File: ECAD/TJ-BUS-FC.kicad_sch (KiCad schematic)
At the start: 31 parts

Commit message: teensy lib
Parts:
- removed A?: (no value), symbol 9602N:9602N
- removed AE?: (no value), symbol Device:Antenna_Shield
- removed C? (x8): (no value), symbol Device:C
- removed C? (x2): (no value), symbol Device:C_Polarized
- removed L?: (no value), symbol Device:L
- removed R? (x2): (no value), symbol Device:R
- removed TP? (x2): (no value), symbol Connector:TestPoint
- removed TP? (x2): (no value), symbol Connector:TestPoint_2Pole
- removed U?: (no value), symbol Amplifier_Current:INA138
- removed U?: (no value), symbol Symbols:MAX17644
- added U?: Teensy4.1, symbol teensy:Teensy4.1
- added U?: DS3232M, Package_SO:SOIC-8_3.9x4.9mm_P1.27mm, symbol Timer_RTC:DS3232M
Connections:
- no-connect marks 11 -> 8
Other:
- added sheet Radio (Iridium.kicad_sch)
- note removed: "750KHz selected"
- note removed: "8ms soft start"
- note removed: "All logic is 3.3V logic level, but is 5V tolerant TX and RX are from master device (TX is input to the 9602, RX is output from the 9602)"
- note removed: "DCM Mode"
- note removed: "Low ESR MLCC + Tantalum Bulk Capacitance"
- note removed: "Probe here to check internal 3V3"
- note removed: "Specced 18V max input"
- note removed: "Synchronous Buck - Stable 5V Out, 2.7A current limit"
- note removed: "This thing is really picky about power: 5V, <100mVpp 0-50KHz, <10mVpp 1MHz, <5mVpp 5Mhz Transients spikes during xmit from 40mA (idle) to 1.5A (xmit) for 8.3ms Cannot droop below 4.8V during this time OCP required, and in-rush current limit to 4A"

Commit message: bno055
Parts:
- added U?: (no value), symbol Symbols:Adafruit BNO055
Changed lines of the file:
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@@
     (pin "8")
+  )
+  (symbol (lib_id "Symbols:Adafruit BNO055") (at 207.01 69.85 0) (unit 1)
+    (in_bom yes) (on_board yes) (fields_autoplaced)
+    (property "Reference" "U?" (id 0) (at 207.01 64.77 0))
+    (property "Value" "" (id 1) (at 207.01 67.31 0))
+    (property "Footprint" "" (id 2) (at 207.01 69.85 0)
+      (effects (font (size 1.27 1.27)) hide)
+    )
+    (property "Datasheet" "" (id 3) (at 207.01 69.85 0)
+      (effects (font (size 1.27 1.27)) hide)
+    )
+    (pin "1")
+    (pin "10")
+    (pin "2")
+    (pin "3")
+    (pin "4")
+    (pin "5")
+    (pin "6")
+    (pin "7")
+    (pin "8")
+    (pin "9")
   )
   (sheet (at 238.76 30.48) (size 20.32 10.16) (fields_autoplaced)
@@
       (reference "U?") (unit 1) (value "DS3232M") (footprint "Package_SO:SOIC-8_3.9x4.9mm_P1.27mm")
     )
-  )
+    (path "/cfd6d7d9-e276-49ef-829b-32515e258b69"
+      (reference "U?") (unit 1) (value "Adafruit BNO055") (footprint "")
+    )
+  )

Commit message: changes
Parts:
- U?: value (none) -> Adafruit BNO055
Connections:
- net +5V: now also U?.48 (VIN)
- net at U?.34 (GND): now also U?.47 (GND)
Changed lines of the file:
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@@
   (no_connect (at 327.66 96.52))
   (no_connect (at 327.66 76.2))
+  (wire (pts (xy 54.61 55.88) (xy 59.69 55.88))
+    (stroke (width 0) (type default) (color 0 0 0 0))
+  )
   (wire (pts (xy 306.07 73.66) (xy 306.07 83.82))
     (stroke (width 0) (type default) (color 0 0 0 0))
@@
     (stroke (width 0) (type default) (color 0 0 0 0))
   )
+  (wire (pts (xy 115.57 55.88) (xy 119.38 55.88))
+    (stroke (width 0) (type default) (color 0 0 0 0))
+  )
+  (wire (pts (xy 115.57 91.44) (xy 133.35 91.44))
+    (stroke (width 0) (type default) (color 0 0 0 0))
+  )
   (wire (pts (xy 327.66 86.36) (xy 336.55 86.36))
     (stroke (width 0) (type default) (color 0 0 0 0))
@@
     (stroke (width 0) (type default) (color 0 0 0 0))
   )
+  (wire (pts (xy 115.57 58.42) (xy 133.35 58.42))
+    (stroke (width 0) (type default) (color 0 0 0 0))
+  )
   (wire (pts (xy 327.66 83.82) (xy 336.55 83.82))
     (stroke (width 0) (type default) (color 0 0 0 0))
@@
   )
   (wire (pts (xy 314.96 73.66) (xy 306.07 73.66))
+    (stroke (width 0) (type default) (color 0 0 0 0))
+  )
+  (wire (pts (xy 133.35 91.44) (xy 133.35 58.42))
     (stroke (width 0) (type default) (color 0 0 0 0))
   )
@@
     (pin "4")
   )
+  (symbol (lib_id "power:+5V") (at 119.38 55.88 0) (unit 1)
+    (in_bom yes) (on_board yes)
+    (property "Reference" "#PWR?" (id 0) (at 119.38 59.69 0)
+      (effects (font (size 1.27 1.27)) hide)
+    )
+    (property "Value" "+5V" (id 1) (at 119.761 52.6288 90)
+      (effects (font (size 1.27 1.27)) (justify left))
+    )
+    (property "Footprint" "" (id 2) (at 119.38 55.88 0)
+      (effects (font (size 1.27 1.27)) hide)
+    )
+    (property "Datasheet" "" (id 3) (at 119.38 55.88 0)
+      (effects (font (size 1.27 1.27)) hide)
+    )
+    (pin "1")
+  )
   (symbol (lib_id "Timer_RTC:DS3232M") (at 156.21 60.96 0) (unit 1)
     (in_bom yes) (on_board yes) (fields_autoplaced)
@@
     (in_bom yes) (on_board yes) (fields_autoplaced)
     (property "Reference" "U?" (id 0) (at 207.01 64.77 0))
-    (property "Value" "" (id 1) (at 207.01 67.31 0))
+    (property "Value" "Adafruit BNO055" (id 1) (at 207.01 67.31 0))
     (property "Footprint" "" (id 2) (at 207.01 69.85 0)
       (effects (font (size 1.27 1.27)) hide)
@@
       (reference "#PWR0112") (unit 1) (value "GND") (footprint "")
     )
+    (path "/3e308dc9-2a7e-453c-9c0d-ed6716a1e4ef"
+      (reference "#PWR?") (unit 1) (value "+5V") (footprint "")
+    )
     (path "/1b0ebad7-8a43-40a6-b997-58eed2589c95/3eb05901-ffe5-47bb-9f32-cde382bc7740"

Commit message: RTC
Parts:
- added BT?: (no value), symbol Device:Battery_Cell
- added C?: 1uF, symbol Device:C
- added C?: (no value), symbol Device:C
- added TP?: (no value), symbol Connector:TestPoint
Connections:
- net +3V3: now also U?.2 (VCC), C?.1
- net GND: now also U?.5 (GND), BT?.2 (-), C?.2, C?.2
- net SCL0: now also U?.8 (SCL)
- net SDA0: now also U?.7 (SDA)
- net at U?.34 (GND): no longer U?.47 (GND)
- net at U?.3 (~{INT}/SQW): now also TP?.1
- net at U?.6 (VBAT): now also BT?.1 (+), C?.1
- no-connect marks 8 -> 10
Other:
- moved on the sheet: U?

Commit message: gpio
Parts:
- added J?: (no value), symbol Connector:Conn_01x02_Female
- BT?: value (none) -> CR2032
- C?: value (none) -> 1uF
- TP?: value (none) -> SQWV
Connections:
- net 5VIN: now also J?.1 (Pin_1)
- net CRX3/GP30: now also U?.22 (30_CRX3)
- net CS/GP10: now also U?.12 (10_CS_MQSR)
- net CS/GP36: now also U?.28 (36_CS)
- net CS/GP37: now also U?.29 (37_CS)
- net CTX3/GP31: now also U?.23 (31_CTX3)
- net GND: now also U?.1 (GND), U?.34 (GND), U?.47 (GND), U?.52 (GND), U?.58 (GND), U?.59 (GND), U?.64 (GND), J?.2 (Pin_2)
- net GP14/A0/TX3: now also U?.36 (14_A0_TX3_SPDIF_OUT)
- net GP15/A1/RX3: now also U?.37 (15_A1_RX3_SPDIF_IN)
- net GP2: now also U?.4 (2_OUT2)
- net GP20/A6/TX5: now also U?.42 (20_A6_TX5_LRCLK1)
- net GP21/A7/RX5: now also U?.43 (21_A7_RX5_BCLK1)
- net GP22/A8: now also U?.44 (22_A8_CTX1)
- net GP23/A9: now also U?.45 (23_A9_CRX1_MCLK1)
- net GP3: now also U?.5 (3_LRCLK2)
- net GP32: now also U?.24 (32_OUT1B)
- net GP33: now also U?.25 (33_MCLK2)
- net GP38/A14: now also U?.30 (38_CS1_IN1)
- net GP4: now also U?.6 (4_BCLK2)
- net GP40/A16: now also U?.32 (40_A16)
- net GP41/A17: now also U?.33 (41_A17)
- net GP5: now also U?.7 (5_IN2)
- net GP6: now also U?.8 (6_OUT1D)
- net GP9: now also U?.11 (9_OUT1C)
- net MISO0: now also U?.14 (12_MISO_MQSL)
- net MISO1: now also U?.31 (39_MISO1_OUT1A)
- net MOSI0: now also U?.13 (11_MOSI_CTX1)
- net MOSI1: now also U?.18 (26_A12_MOSI1)
- net RX1/GP0: now also U?.2 (0_RX1_CRX2_CS1)
- net RX2/GP7: now also U?.9 (7_RX2_OUT1A)
- net RX7/GP28: now also U?.20 (28_RX7)
- net RX8/GP34: now also U?.26 (34_RX8)
- net SCK0: now also U?.35 (13_SCK_LED)
- net SCK1: now also U?.19 (27_A13_SCK1)
- net SCL0: now also U?.41 (19_A5_SCL)
- net SCL1: now also U?.38 (16_A2_RX4_SCL1)
- net SCL2: now also U?.16 (24_A10_TX6_SCL2)
- net SDA0: now also U?.40 (18_A4_SDA)
- net SDA1: now also U?.39 (17_A3_TX4_SDA1)
- net SDA2: now also U?.17 (25_A11_RX6_SDA2)
- net TX1/GP1: now also U?.3 (1_TX1_CTX2_MISO1)
- net TX2/GP8: now also U?.10 (8_TX2_IN1)
- net TX7/GP29: now also U?.21 (29_TX7)
- net TX8/GP35: now also U?.27 (35_TX8)
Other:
- moved on the sheet: BT?, C?, TP?, U?

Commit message: minor fix
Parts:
- J?: value (none) -> PWR
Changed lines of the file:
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@@
       (effects (font (size 1.27 1.27)) (justify left))
     )
-    (property "Value" "" (id 1) (at 274.32 133.3499 0)
+    (property "Value" "PWR" (id 1) (at 274.32 133.3499 0)
       (effects (font (size 1.27 1.27)) (justify left))
     )
@@
       (effects (font (size 1.27 1.27)) hide)
     )
-    (property "Value" "" (id 1) (at 267.97 138.43 0))
+    (property "Value" "GND" (id 1) (at 267.97 138.43 0))
     (property "Footprint" "" (id 2) (at 267.97 133.35 0)
       (effects (font (size 1.27 1.27)) hide)

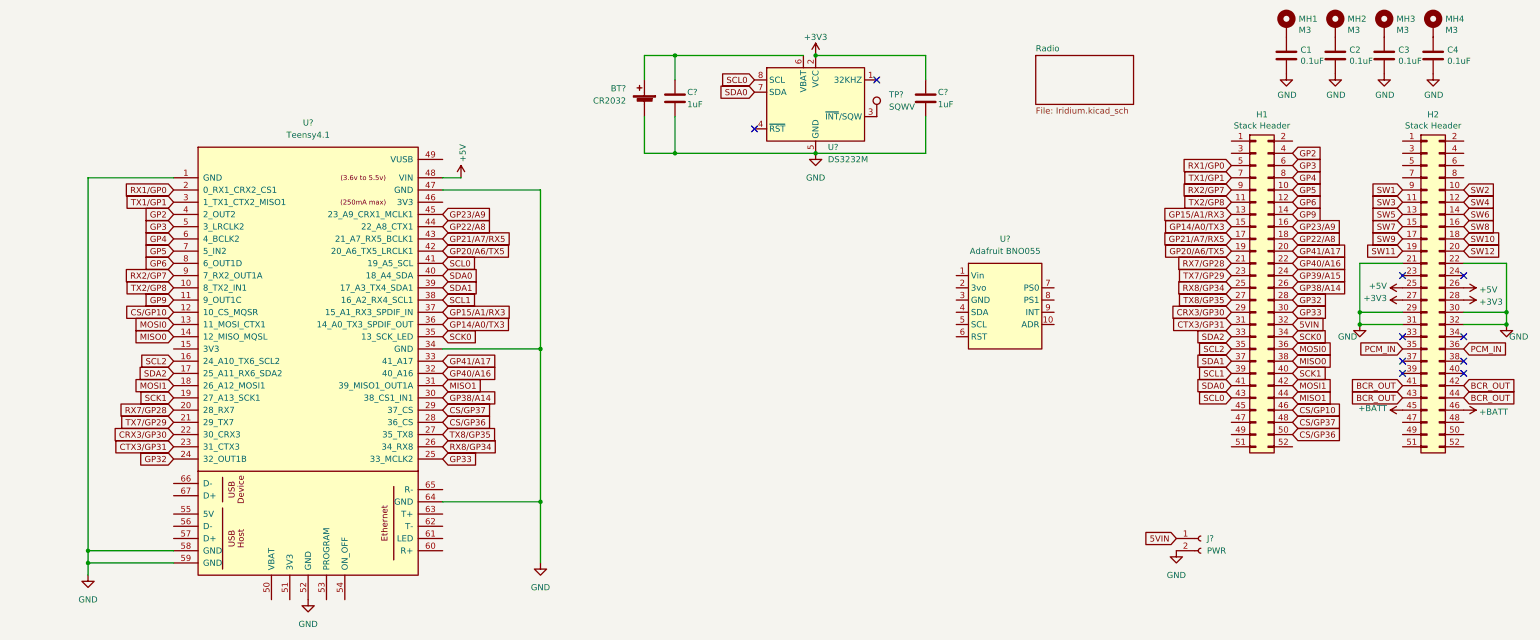
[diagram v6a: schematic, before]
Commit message: fram module and preliminary linking
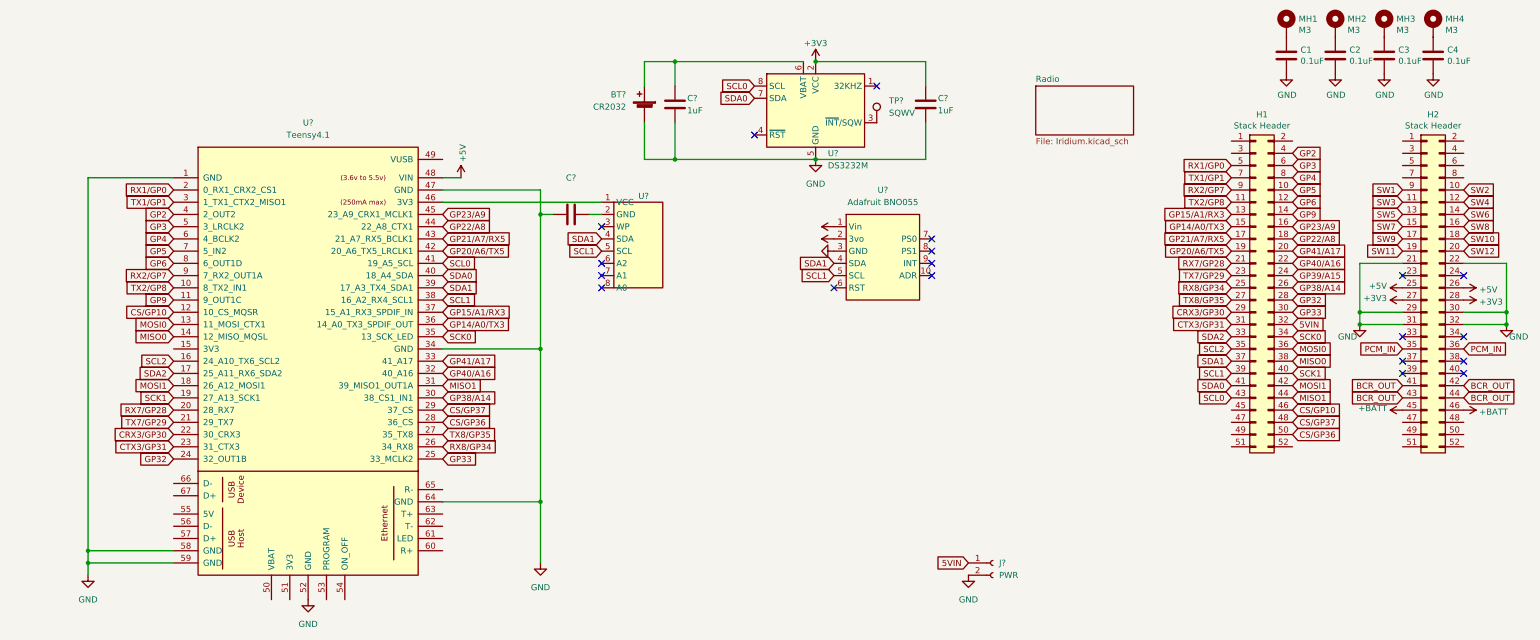
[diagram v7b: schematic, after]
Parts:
- added C?: (no value), symbol Device:C
- added U?: (no value), symbol Symbols:Adafruit_FRAM
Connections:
- net +3V3: now also U?.1 (Vin), U?.2 (3vo)
- net GND: now also U?.3 (GND), C?.1
- net SCL1: now also U?.5 (SCL), U?.5 (SCL)
- net SDA1: now also U?.4 (SDA), U?.4 (SDA)
- net at U?.46 (3V3): now also U?.1 (VCC)
- new net: C?.2, U?.2 (GND)
- no-connect marks 10 -> 19
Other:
- moved on the sheet: BT?, C?, J?, TP?, U?

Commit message: remove 5VIN
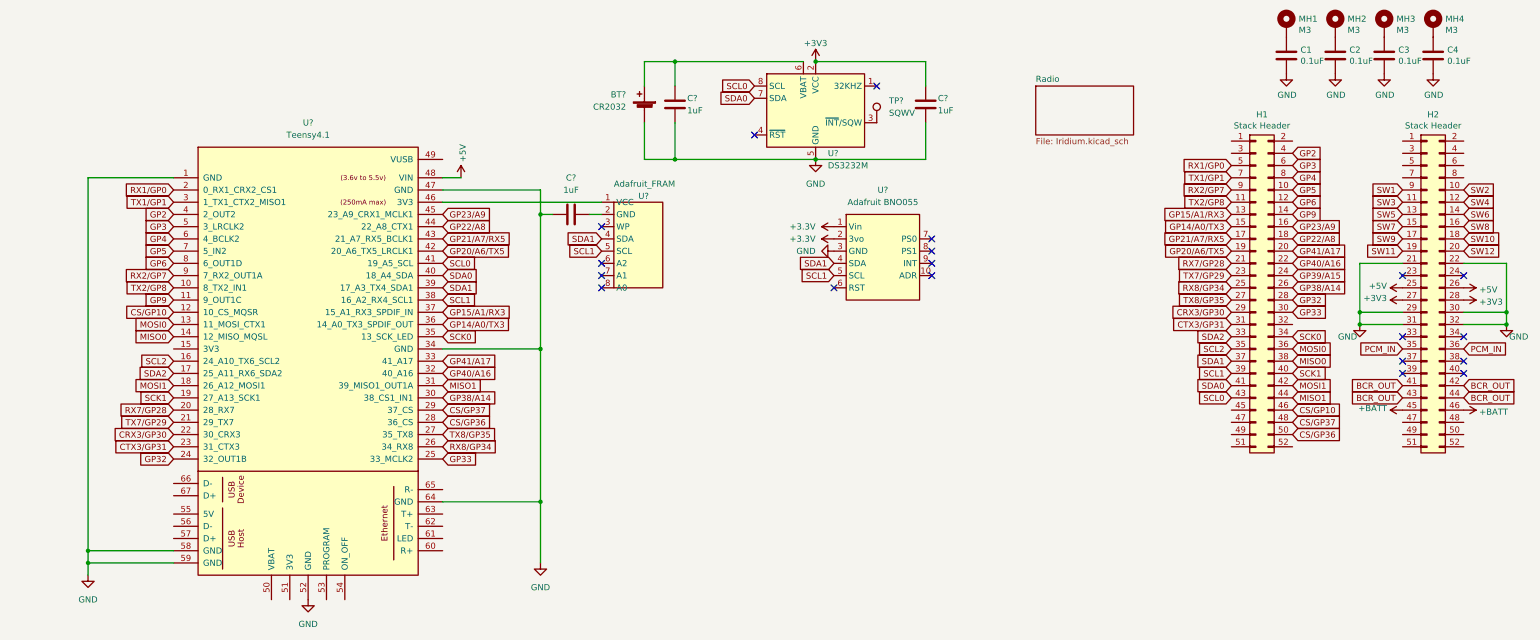
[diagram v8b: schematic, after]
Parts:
- removed J?: PWR, symbol Connector:Conn_01x02_Female
- C?: value (none) -> 1uF
- U?: value (none) -> Adafruit_FRAM
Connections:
- net 5VIN: no longer names the net of H1.32 (Pin_32)
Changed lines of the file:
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@@
-    )
-  )
-  (global_label "5VIN" (shape input) (at 224.79 135.89 180) (fields_autoplaced)
-    (effects (font (size 1.27 1.27)) (justify right))
-    (property "Intersheet References" "${INTERSHEET_REFS}" (id 0) (at 462.28 220.98 0)
-      (effects (font (size 1.27 1.27)) hide)
     )
   )
@@
     (property "Intersheet References" "${INTERSHEET_REFS}" (id 0) (at 304.2213 78.6606 0)
       (effects (font (size 1.27 1.27)) (justify left) hide)
-    )
-  )
-  (global_label "5VIN" (shape input) (at 292.1 86.36 0) (fields_autoplaced)
-    (effects (font (size 1.27 1.27)) (justify left))
-    (property "Intersheet References" "${INTERSHEET_REFS}" (id 0) (at 54.61 1.27 0)
-      (effects (font (size 1.27 1.27)) hide)
     )
   )
@@
       (effects (font (size 1.27 1.27)) (justify left))
     )
-    (property "Value" "" (id 1) (at 151.13 57.15 90)
+    (property "Value" "Adafruit_FRAM" (id 1) (at 151.13 57.15 90)
       (effects (font (size 1.27 1.27)) (justify left))
     )
@@
     (in_bom yes) (on_board yes) (fields_autoplaced)
     (property "Reference" "C?" (id 0) (at 142.24 55.88 90))
-    (property "Value" "" (id 1) (at 142.24 58.42 90))
+    (property "Value" "1uF" (id 1) (at 142.24 58.42 90))
     (property "Footprint" "" (id 2) (at 146.05 62.5348 0)
       (effects (font (size 1.27 1.27)) hide)
@@
     (pin "8")
   )
-  (symbol (lib_id "Connector:Conn_01x02_Female") (at 229.87 135.89 0) (unit 1)
-    (in_bom yes) (on_board yes) (fields_autoplaced)
-    (property "Reference" "J?" (id 0) (at 231.14 135.8899 0)
-      (effects (font (size 1.27 1.27)) (justify left))
-    )
-    (property "Value" "PWR" (id 1) (at 231.14 138.4299 0)
-      (effects (font (size 1.27 1.27)) (justify left))
-    )
-    (property "Footprint" "" (id 2) (at 229.87 135.89 0)
-      (effects (font (size 1.27 1.27)) hide)
-    )
-    (property "Datasheet" "~" (id 3) (at 229.87 135.89 0)
-      (effects (font (size 1.27 1.27)) hide)
-    )
-    (pin "1")
-    (pin "2")
-  )
   (symbol (lib_id "power:GND") (at 193.04 52.07 0) (unit 1)
     (in_bom yes) (on_board yes)
@@
     )
     (property "Datasheet" "~" (id 3) (at 210.82 44.45 0)
-      (effects (font (size 1.27 1.27)) hide)
-    )
-    (pin "1")
-  )
-  (symbol (lib_id "power:GND") (at 224.79 138.43 0) (unit 1)
-    (in_bom yes) (on_board yes) (fields_autoplaced)
-    (property "Reference" "#PWR?" (id 0) (at 224.79 144.78 0)
-      (effects (font (size 1.27 1.27)) hide)
-    )
-    (property "Value" "GND" (id 1) (at 224.79 143.51 0))
-    (property "Footprint" "" (id 2) (at 224.79 138.43 0)
-      (effects (font (size 1.27 1.27)) hide)
-    )
-    (property "Datasheet" "" (id 3) (at 224.79 138.43 0)
       (effects (font (size 1.27 1.27)) hide)
     )
@@
       (effects (font (size 1.27 1.27)) hide)
     )
-    (property "Value" "" (id 1) (at 193.04 66.0399 90)
+    (property "Value" "+3.3V" (id 1) (at 193.04 66.0399 90)
       (effects (font (size 1.27 1.27)) (justify left))
     )
@@
       (effects (font (size 1.27 1.27)) hide)
     )
-    (property "Value" "" (id 1) (at 193.04 71.1199 90)
+    (property "Value" "GND" (id 1) (at 193.04 71.1199 90)
       (effects (font (size 1.27 1.27)) (justify right))
     )
@@
       (effects (font (size 1.27 1.27)) hide)
     )
-    (property "Value" "" (id 1) (at 193.04 68.5799 90)
+    (property "Value" "+3.3V" (id 1) (at 193.04 68.5799 90)
       (effects (font (size 1.27 1.27)) (justify left))
     )
@@
       (reference "#PWR?") (unit 1) (value "GND") (footprint "")
     )
-    (path "/ada2bafc-40cb-4d29-9269-ce160ab48fcc"
-      (reference "#PWR?") (unit 1) (value "GND") (footprint "")
-    )
     (path "/1b0ebad7-8a43-40a6-b997-58eed2589c95/ba16728d-3684-42ae-a4d8-298c4a006593"
       (reference "#PWR?") (unit 1) (value "GND") (footprint "")
@@
       (reference "H2") (unit 1) (value "Stack Header") (footprint "Connector_PinHeader_2.54mm:PinHeader_2x26_P2.54mm_Vertical")
     )
-    (path "/8142001c-a9d5-457a-9968-95120d035d39"
-      (reference "J?") (unit 1) (value "PWR") (footprint "")
-    )
     (path "/1b0ebad7-8a43-40a6-b997-58eed2589c95/2c8c9572-9c16-41b9-81dc-5ea6c5fa6361"
